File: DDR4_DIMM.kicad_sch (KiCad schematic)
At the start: 0 parts

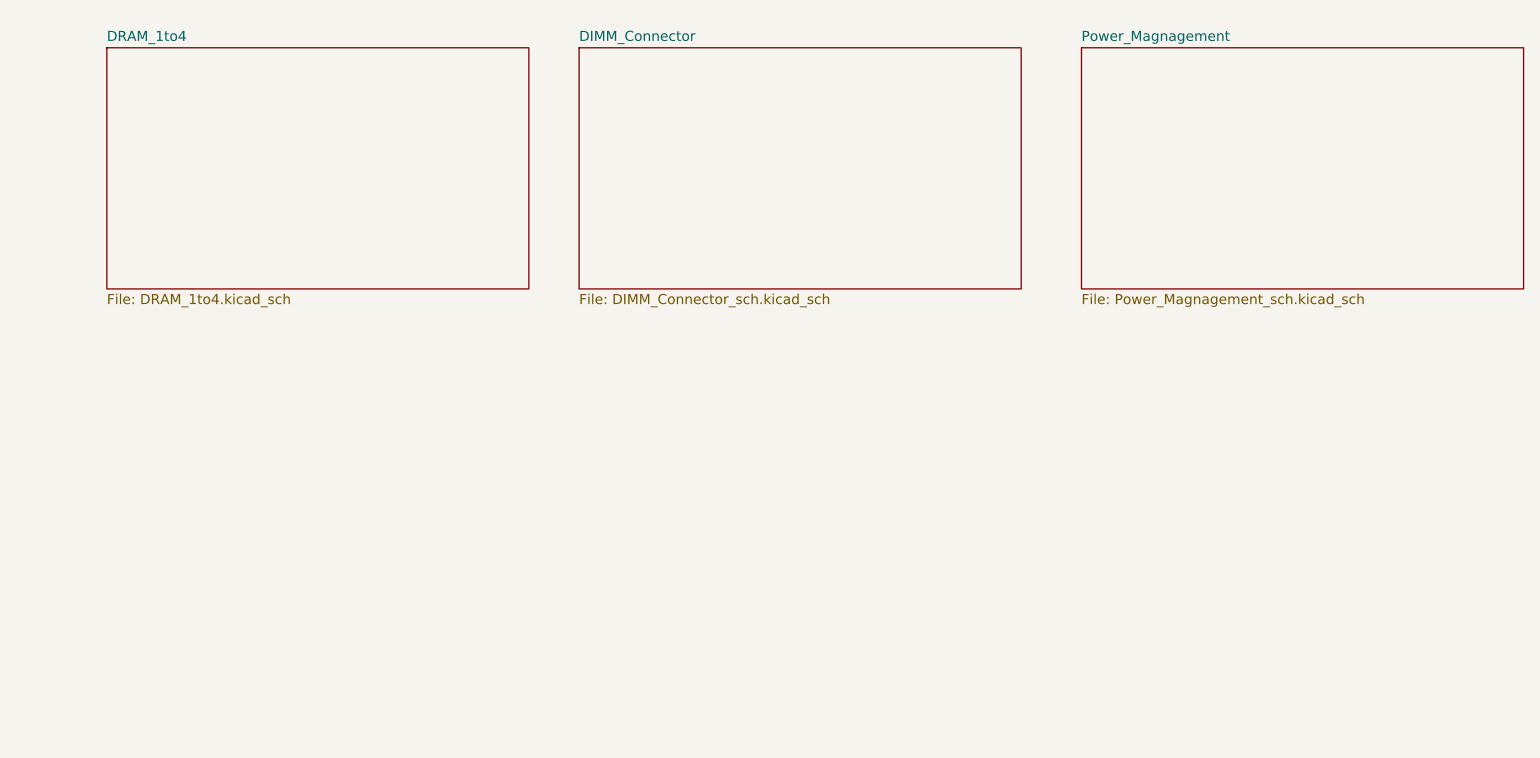
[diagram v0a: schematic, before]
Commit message: Update schametic 1. Adding 7 DRAMS, 2. Replacing a SPD EEPROM with new one that is including in a temperature sensor, 3. modifying a DIMM Connector and DRAM PAD
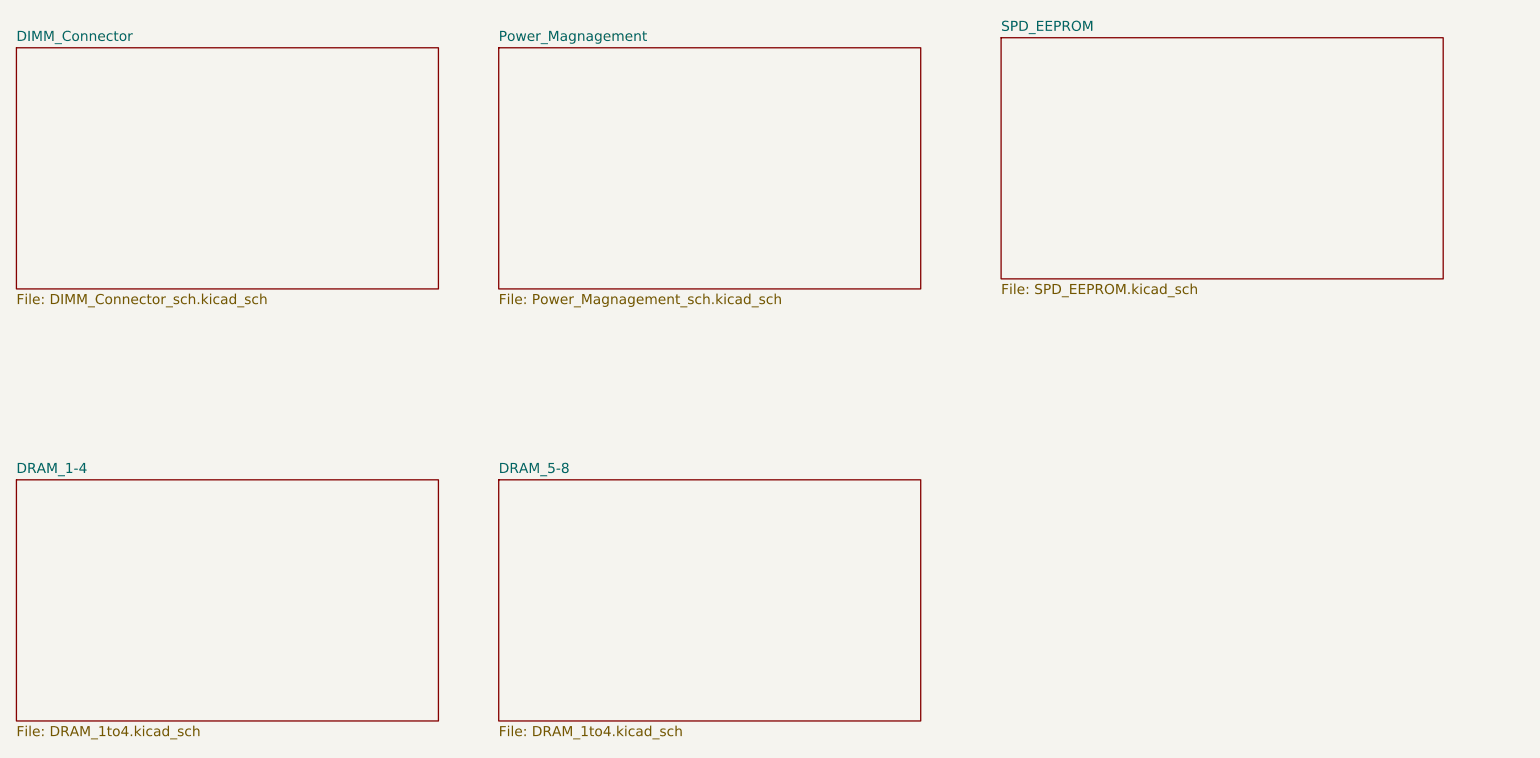
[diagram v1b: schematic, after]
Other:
- sheet DRAM_1to4 renamed DRAM_1-4
- added sheet DRAM_5-8 (DRAM_1to4.kicad_sch)
- added sheet SPD_EEPROM (SPD_EEPROM.kicad_sch)
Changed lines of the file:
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@@
 	(paper "A4")
 	(sheet
-		(at 91.44 33.02)
+		(at 81.28 87.63)
+		(size 53.34 30.48)
+		(exclude_from_sim no)
+		(in_bom yes)
+		(on_board yes)
+		(dnp no)
+		(fields_autoplaced yes)
+		(stroke
+			(width 0.1524)
+			(type solid)
+		)
+		(fill
+			(color 0 0 0 0)
+		)
+		(property "Sheetname" "DRAM_5-8"
+			(at 81.28 86.9184 0)
+			(show_name no)
+			(do_not_autoplace no)
+			(effects
+				(font
+					(size 1.27 1.27)
+				)
+				(justify left bottom)
+			)
+		)
+		(property "Sheetfile" "DRAM_1to4.kicad_sch"
+			(at 81.28 118.6946 0)
+			(show_name no)
+			(do_not_autoplace no)
+			(effects
+				(font
+					(size 1.27 1.27)
+				)
+				(justify left top)
+			)
+		)
+		(instances
+			(project "DDR4_DIMM"
+				(path "/2162f80d-5bbc-406a-8824-9611d78b7103"
+					(page "4")
+				)
+			)
+		)
+	)
+	(sheet
+		(at 20.32 33.02)
+		(size 53.34 30.48)
+		(exclude_from_sim no)
+		(in_bom yes)
+		(on_board yes)
+		(dnp no)
+		(fields_autoplaced yes)
+		(stroke
+			(width 0.1524)
+			(type solid)
+		)
+		(fill
+			(color 0 0 0 0)
+		)
+		(property "Sheetname" "DIMM_Connector"
+			(at 20.32 32.3084 0)
+			(show_name no)
+			(do_not_autoplace no)
+			(effects
+				(font
+					(size 1.27 1.27)
+				)
+				(justify left bottom)
+			)
+		)
+		(property "Sheetfile" "DIMM_Connector_sch.kicad_sch"
+			(at 20.32 64.0846 0)
+			(show_name no)
+			(do_not_autoplace no)
+			(effects
+				(font
+					(size 1.27 1.27)
+				)
+				(justify left top)
+			)
+		)
+		(instances
+			(project "DDR4_DIMM"
+				(path "/2162f80d-5bbc-406a-8824-9611d78b7103"
+					(page "2")
+				)
+			)
+		)
+	)
+	(sheet
+		(at 20.32 87.63)
+		(size 53.34 30.48)
+		(exclude_from_sim no)
+		(in_bom yes)
+		(on_board yes)
+		(dnp no)
+		(fields_autoplaced yes)
+		(stroke
+			(width 0.1524)
+			(type solid)
+		)
+		(fill
+			(color 0 0 0 0)
+		)
+		(property "Sheetname" "DRAM_1-4"
+			(at 20.32 86.9184 0)
+			(show_name no)
+			(do_not_autoplace no)
+			(effects
+				(font
+					(size 1.27 1.27)
+				)
+				(justify left bottom)
+			)
+		)
+		(property "Sheetfile" "DRAM_1to4.kicad_sch"
+			(at 20.32 118.6946 0)
+			(show_name no)
+			(do_not_autoplace no)
+			(effects
+				(font
+					(size 1.27 1.27)
+				)
+				(justify left top)
+			)
+		)
+		(instances
+			(project "DDR4_DIMM"
+				(path "/2162f80d-5bbc-406a-8824-9611d78b7103"
+					(page "3")
+				)
+			)
+		)
+	)
+	(sheet
+		(at 144.78 31.75)
 		(size 55.88 30.48)
 		(exclude_from_sim no)
@@
 			(color 0 0 0 0)
 		)
-		(property "Sheetname" "DIMM_Connector"
-			(at 91.44 32.3084 0)
-			(show_name no)
-			(do_not_autoplace no)
-			(effects
-				(font
-					(size 1.27 1.27)
-				)
-				(justify left bottom)
-			)
-		)
-		(property "Sheetfile" "DIMM_Connector_sch.kicad_sch"
-			(at 91.44 64.0846 0)
-			(show_name no)
-			(do_not_autoplace no)
-			(effects
-				(font
-					(size 1.27 1.27)
-				)
-				(justify left top)
-			)
-		)
-		(instances
-			(project "DDR4_DIMM"
-				(path "/2162f80d-5bbc-406a-8824-9611d78b7103"
-					(page "3")
-				)
-			)
-		)
-	)
-	(sheet
-		(at 31.75 33.02)
-		(size 53.34 30.48)
-		(exclude_from_sim no)
-		(in_bom yes)
-		(on_board yes)
-		(dnp no)
-		(fields_autoplaced yes)
-		(stroke
-			(width 0.1524)
-			(type solid)
-		)
-		(fill
-			(color 0 0 0 0)
-		)
-		(property "Sheetname" "DRAM_1to4"
-			(at 31.75 32.3084 0)
-			(show_name no)
-			(do_not_autoplace no)
-			(effects
-				(font
-					(size 1.27 1.27)
-				)
-				(justify left bottom)
-			)
-		)
-		(property "Sheetfile" "DRAM_1to4.kicad_sch"
-			(at 31.75 64.0846 0)
-			(show_name no)
-			(do_not_autoplace no)
-			(effects
-				(font
-					(size 1.27 1.27)
-				)
-				(justify left top)
-			)
-		)
-		(instances
-			(project "DDR4_DIMM"
-				(path "/2162f80d-5bbc-406a-8824-9611d78b7103"
-					(page "2")
-				)
-			)
-		)
-	)
-	(sheet
-		(at 154.94 33.02)
-		(size 55.88 30.48)
+		(property "Sheetname" "SPD_EEPROM"
+			(at 144.78 31.0384 0)
+			(show_name no)
+			(do_not_autoplace no)
+			(effects
+				(font
+					(size 1.27 1.27)
+				)
+				(justify left bottom)
+			)
+		)
+		(property "Sheetfile" "SPD_EEPROM.kicad_sch"
+			(at 144.78 62.8146 0)
+			(show_name no)
+			(do_not_autoplace no)
+			(effects
+				(font
+					(size 1.27 1.27)
+				)
+				(justify left top)
+			)
+		)
+		(instances
+			(project "DDR4_DIMM"
+				(path "/2162f80d-5bbc-406a-8824-9611d78b7103"
+					(page "6")
+				)
+			)
+		)
+	)
+	(sheet
+		(at 81.28 33.02)
+		(size 53.34 30.48)
 		(exclude_from_sim no)
 		(in_bom yes)
@@
 		)
 		(property "Sheetname" "Power_Magnagement"
-			(at 154.94 32.3084 0)
+			(at 81.28 32.3084 0)
 			(show_name no)
 			(do_not_autoplace no)
@@
 		)
 		(property "Sheetfile" "Power_Magnagement_sch.kicad_sch"
-			(at 154.94 64.0846 0)
-			(show_name no)
-			(do_not_autoplace no)
-			(effects
-				(font
-					(size 1.27 1.27)
-				)
-				(justify left top)
-			)
-		)
-		(instances
-			(project "DDR4_DIMM"
-				(path "/2162f80d-5bbc-406a-8824-9611d78b7103"
-					(page "4")
-				)
-			)
+			(at 81.28 64.0846 0)
+			(show_name no)
+			(do_not_autoplace no)
+			(effects
+				(font
+					(size 1.27 1.27)
+				)
+				(justify left top)
+			)
+		)
+		(instances
+			(project "DDR4_DIMM"
+				(path "/2162f80d-5bbc-406a-8824-9611d78b7103"
+					(page "5")
+				)
+			)

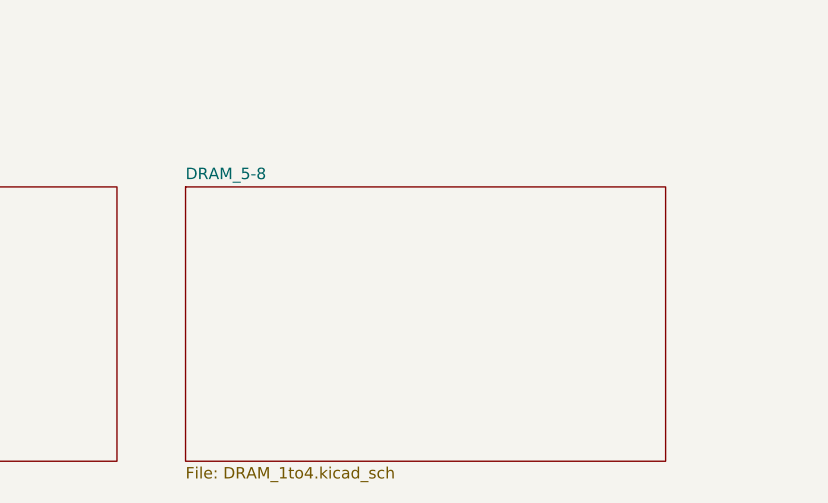
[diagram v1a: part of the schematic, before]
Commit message: Modifying stack up from 8 layers to 6 layers and DRAM 5-8 Schematic restore.
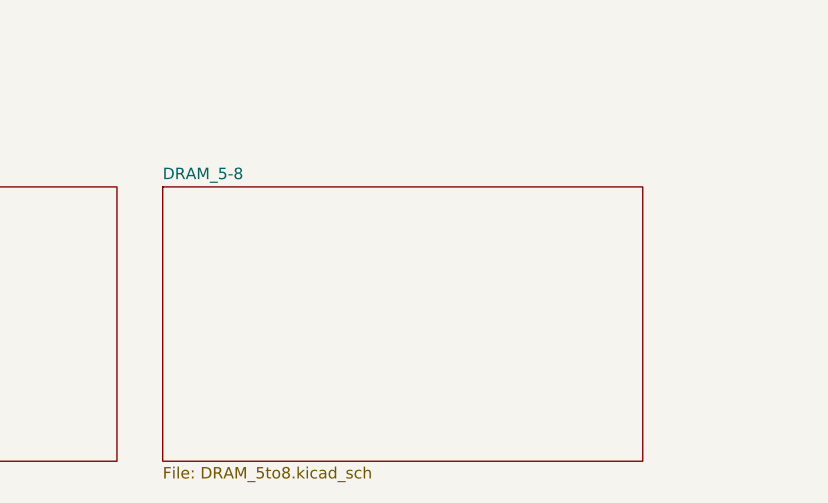
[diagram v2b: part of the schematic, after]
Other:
- sheet DRAM_5-8: file DRAM_1to4.kicad_sch -> DRAM_5to8.kicad_sch
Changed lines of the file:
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@@
 	(paper "A4")
-	(sheet
-		(at 81.28 87.63)
-		(size 53.34 30.48)
-		(exclude_from_sim no)
-		(in_bom yes)
-		(on_board yes)
-		(dnp no)
-		(fields_autoplaced yes)
-		(stroke
-			(width 0.1524)
-			(type solid)
-		)
-		(fill
-			(color 0 0 0 0)
-		)
-		(property "Sheetname" "DRAM_5-8"
-			(at 81.28 86.9184 0)
-			(show_name no)
-			(do_not_autoplace no)
-			(effects
-				(font
-					(size 1.27 1.27)
-				)
-				(justify left bottom)
-			)
-		)
-		(property "Sheetfile" "DRAM_1to4.kicad_sch"
-			(at 81.28 118.6946 0)
-			(show_name no)
-			(do_not_autoplace no)
-			(effects
-				(font
-					(size 1.27 1.27)
-				)
-				(justify left top)
-			)
-		)
-		(instances
-			(project "DDR4_DIMM"
-				(path "/2162f80d-5bbc-406a-8824-9611d78b7103"
-					(page "4")
-				)
-			)
-		)
-	)
 	(sheet
 		(at 20.32 33.02)
@@
 				)
 			)
+		)
+	)
+	(sheet
+		(at 78.74 87.63)
+		(size 53.34 30.48)
+		(exclude_from_sim no)
+		(in_bom yes)
+		(on_board yes)
+		(dnp no)
+		(fields_autoplaced yes)
+		(stroke
+			(width 0.1524)
+			(type solid)
+		)
+		(fill
+			(color 0 0 0 0)
+		)
+		(property "Sheetname" "DRAM_5-8"
+			(at 78.74 86.9184 0)
+			(show_name no)
+			(do_not_autoplace no)
+			(effects
+				(font
+					(size 1.27 1.27)
+				)
+				(justify left bottom)
+			)
+		)
+		(property "Sheetfile" "DRAM_5to8.kicad_sch"
+			(at 78.74 118.6946 0)
+			(show_name no)
+			(do_not_autoplace no)
+			(effects
+				(font
+					(size 1.27 1.27)
+				)
+				(justify left top)
+			)
+		)
+		(instances
+			(project "DDR4_DIMM"
+				(path "/2162f80d-5bbc-406a-8824-9611d78b7103"
+					(page "4")
+				)
+			)
